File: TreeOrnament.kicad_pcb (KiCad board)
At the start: 2 copper layers, 13 parts, among them J1 USB_B_Micro

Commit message: xmas tree outline
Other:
- board outline added: 20 x 45 mm
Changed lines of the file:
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@@
     (links 18)
     (no_connects 18)
-    (area 0 0 0 0)
+    (area 123.825 100.965 160.875002 124.875)
     (thickness 1.6)
-    (drawings 0)
+    (drawings 5)
     (tracks 0)
     (zones 0)
@@
     )
   )
+  (gr_line (start 125 70) (end 115 85) (angle 90) (layer Edge.Cuts) (width 0.15))
+  (gr_line (start 120 70) (end 125 70) (angle 90) (layer Edge.Cuts) (width 0.15))
+  (gr_line (start 130 55) (end 120 70) (angle 90) (layer Edge.Cuts) (width 0.15))
+  (gr_line (start 125 55) (end 130 55) (angle 90) (layer Edge.Cuts) (width 0.15))
+  (gr_line (start 135 40) (end 125 55) (angle 90) (layer Edge.Cuts) (width 0.15))
 )

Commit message: draw the tree
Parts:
- J1: moved to B.Cu
- moved D5 59.0 mm to (195.0, 150.0)
- moved D2 50.0 mm to (165.4, 159.0)
- moved D1 50.0 mm to (176.4, 144.9)
- moved D3 50.0 mm to (181.7, 144.9)
- moved D4 50.0 mm to (175.6, 152.9)
- moved D6 50.0 mm to (180.9, 152.9)
- moved D7 50.0 mm to (170.7, 160.8)
- moved D8 50.0 mm to (186.2, 152.9)
- moved R1 19.5 mm to (115.0, 95.0), turned to 330 degrees
- moved R3 16.6 mm to (135.0, 105.0), turned to 330 degrees
- moved J1 16.0 mm to (135.0, 90.0)
- moved R2 11.8 mm to (125.0, 100.0), turned to 330 degrees
- moved R4 9.85 mm to (145.0, 110.0), turned to 330 degrees
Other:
- board size 20 x 45 mm -> 80 x 105 mm

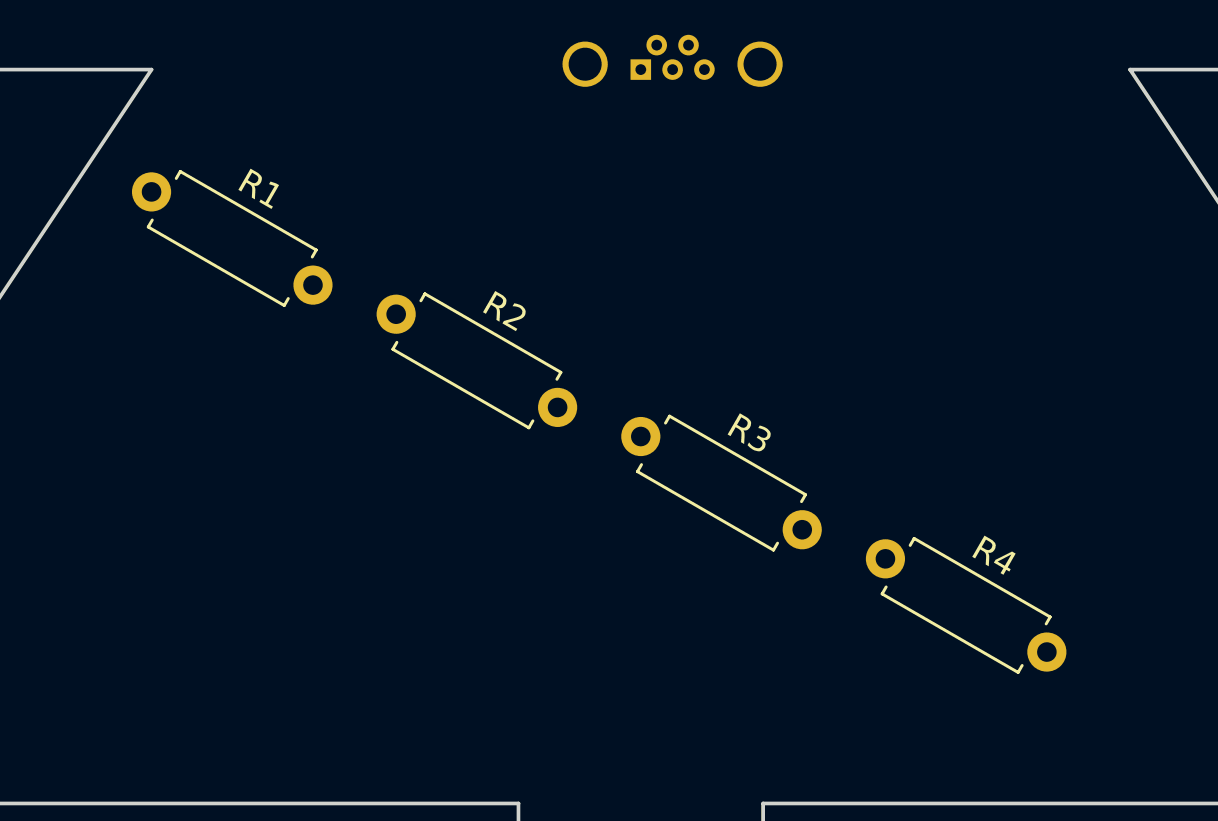
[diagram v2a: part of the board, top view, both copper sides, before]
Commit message: change angle of resistors
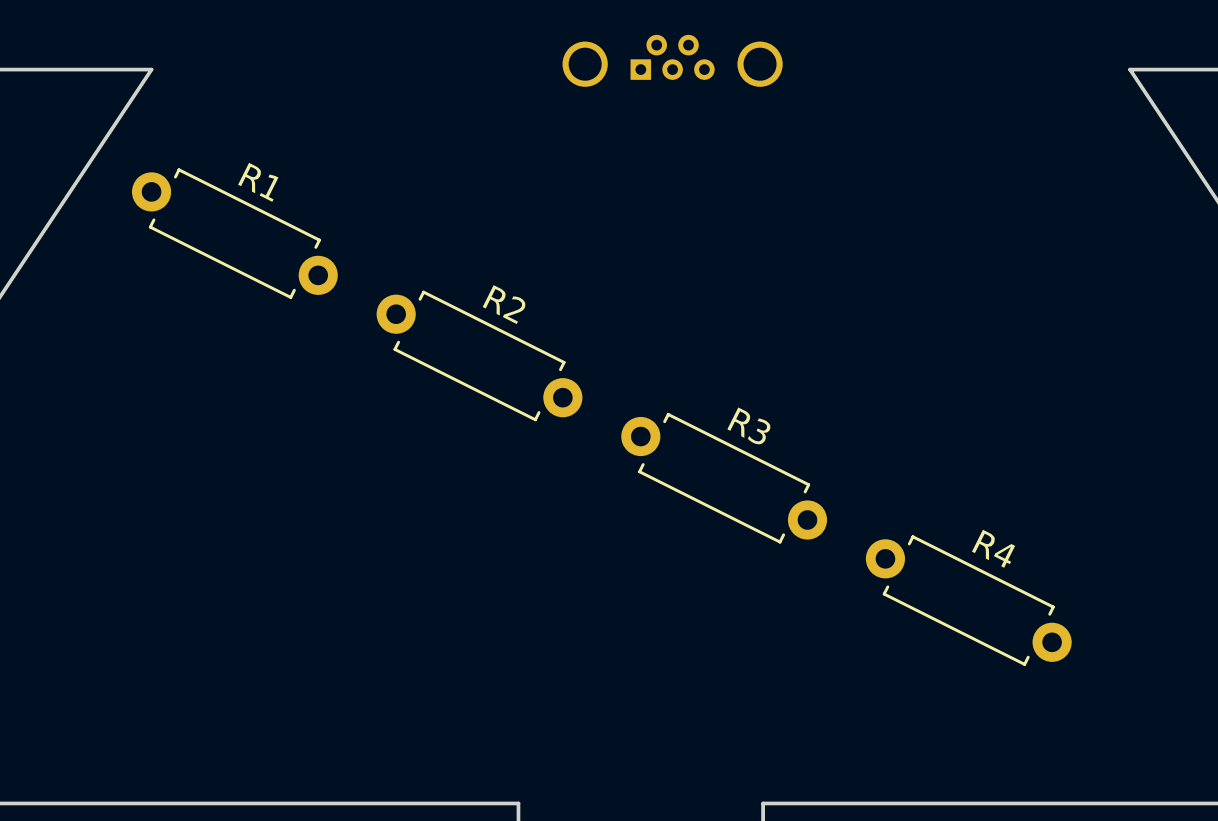
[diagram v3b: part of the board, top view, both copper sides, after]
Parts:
- turned R1 to 333.4 degrees
- turned R2 to 333.4 degrees
- turned R3 to 333.4 degrees
- turned R4 to 333.4 degrees
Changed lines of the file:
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@@
   )
   (module Resistors_THT:R_Axial_DIN0207_L6.3mm_D2.5mm_P7.62mm_Horizontal (layer F.Cu)
-    (at 115 95 330)
+    (at 115 95 333.4)
     (descr "Resistor, Axial_DIN0207 series, Axial, Horizontal, pin pitch=7.62mm, 0.25W = 1/4W, length*diameter=6.3*2.5mm^2, http://cdn-reichelt.de/documents/datenblatt/B400/1_4W%23YAG.pdf")
     (tags "Resistor Axial_DIN0207 series Axial Horizontal pin pitch 7.62mm 0.25W = 1/4W length 6.3mm diameter 2.5mm")
-    (fp_text reference R1 (at 3.81 -2.31 330) (layer F.SilkS)
+    (fp_text reference R1 (at 3.81 -2.31 333.4) (layer F.SilkS)
       (effects (font (size 1 1) (thickness 0.15)))
     )
-    (fp_text value 56 (at 3.81 2.31 330) (layer F.Fab)
+    (fp_text value 56 (at 3.81 2.31 333.4) (layer F.Fab)
       (effects (font (size 1 1) (thickness 0.15)))
     )
@@
     (fp_line (start 8.7 1.6) (end 8.7 -1.6) (layer F.CrtYd) (width 0.05))
     (fp_line (start 8.7 -1.6) (end -1.05 -1.6) (layer F.CrtYd) (width 0.05))
-    (pad 1 thru_hole circle (at 0 0 330) (size 1.6 1.6) (drill 0.8) (layers *.Cu *.Mask)
+    (pad 1 thru_hole circle (at 0 0 333.4) (size 1.6 1.6) (drill 0.8) (layers *.Cu *.Mask)
       (net 10 +5V))
-    (pad 2 thru_hole oval (at 7.62 0 330) (size 1.6 1.6) (drill 0.8) (layers *.Cu *.Mask)
+    (pad 2 thru_hole oval (at 7.62 0 333.4) (size 1.6 1.6) (drill 0.8) (layers *.Cu *.Mask)
       (net 3 "Net-(D2-Pad2)"))
     (model ${KISYS3DMOD}/Resistors_THT.3dshapes/R_Axial_DIN0207_L6.3mm_D2.5mm_P7.62mm_Horizontal.wrl
@@
   )
   (module Resistors_THT:R_Axial_DIN0207_L6.3mm_D2.5mm_P7.62mm_Horizontal (layer F.Cu)
-    (at 125 100 330)
+    (at 125 100 333.4)
     (descr "Resistor, Axial_DIN0207 series, Axial, Horizontal, pin pitch=7.62mm, 0.25W = 1/4W, length*diameter=6.3*2.5mm^2, http://cdn-reichelt.de/documents/datenblatt/B400/1_4W%23YAG.pdf")
     (tags "Resistor Axial_DIN0207 series Axial Horizontal pin pitch 7.62mm 0.25W = 1/4W length 6.3mm diameter 2.5mm")
-    (fp_text reference R2 (at 3.81 -2.31 330) (layer F.SilkS)
+    (fp_text reference R2 (at 3.81 -2.31 333.4) (layer F.SilkS)
       (effects (font (size 1 1) (thickness 0.15)))
     )
-    (fp_text value 56 (at 3.81 2.31 330) (layer F.Fab)
+    (fp_text value 56 (at 3.81 2.31 333.4) (layer F.Fab)
       (effects (font (size 1 1) (thickness 0.15)))
     )
@@
     (fp_line (start 8.7 1.6) (end 8.7 -1.6) (layer F.CrtYd) (width 0.05))
     (fp_line (start 8.7 -1.6) (end -1.05 -1.6) (layer F.CrtYd) (width 0.05))
-    (pad 1 thru_hole circle (at 0 0 330) (size 1.6 1.6) (drill 0.8) (layers *.Cu *.Mask)
+    (pad 1 thru_hole circle (at 0 0 333.4) (size 1.6 1.6) (drill 0.8) (layers *.Cu *.Mask)
       (net 10 +5V))
-    (pad 2 thru_hole oval (at 7.62 0 330) (size 1.6 1.6) (drill 0.8) (layers *.Cu *.Mask)
+    (pad 2 thru_hole oval (at 7.62 0 333.4) (size 1.6 1.6) (drill 0.8) (layers *.Cu *.Mask)
       (net 5 "Net-(D4-Pad2)"))
     (model ${KISYS3DMOD}/Resistors_THT.3dshapes/R_Axial_DIN0207_L6.3mm_D2.5mm_P7.62mm_Horizontal.wrl
@@
   )
   (module Resistors_THT:R_Axial_DIN0207_L6.3mm_D2.5mm_P7.62mm_Horizontal (layer F.Cu)
-    (at 135 105 330)
+    (at 135 105 333.4)
     (descr "Resistor, Axial_DIN0207 series, Axial, Horizontal, pin pitch=7.62mm, 0.25W = 1/4W, length*diameter=6.3*2.5mm^2, http://cdn-reichelt.de/documents/datenblatt/B400/1_4W%23YAG.pdf")
     (tags "Resistor Axial_DIN0207 series Axial Horizontal pin pitch 7.62mm 0.25W = 1/4W length 6.3mm diameter 2.5mm")
-    (fp_text reference R3 (at 3.81 -2.31 330) (layer F.SilkS)
+    (fp_text reference R3 (at 3.81 -2.31 333.4) (layer F.SilkS)
       (effects (font (size 1 1) (thickness 0.15)))
     )
-    (fp_text value 56 (at 3.81 2.31 330) (layer F.Fab)
+    (fp_text value 56 (at 3.81 2.31 333.4) (layer F.Fab)
       (effects (font (size 1 1) (thickness 0.15)))
     )
@@
     (fp_line (start 8.7 1.6) (end 8.7 -1.6) (layer F.CrtYd) (width 0.05))
     (fp_line (start 8.7 -1.6) (end -1.05 -1.6) (layer F.CrtYd) (width 0.05))
-    (pad 1 thru_hole circle (at 0 0 330) (size 1.6 1.6) (drill 0.8) (layers *.Cu *.Mask)
+    (pad 1 thru_hole circle (at 0 0 333.4) (size 1.6 1.6) (drill 0.8) (layers *.Cu *.Mask)
       (net 10 +5V))
-    (pad 2 thru_hole oval (at 7.62 0 330) (size 1.6 1.6) (drill 0.8) (layers *.Cu *.Mask)
+    (pad 2 thru_hole oval (at 7.62 0 333.4) (size 1.6 1.6) (drill 0.8) (layers *.Cu *.Mask)
       (net 7 "Net-(D6-Pad2)"))
     (model ${KISYS3DMOD}/Resistors_THT.3dshapes/R_Axial_DIN0207_L6.3mm_D2.5mm_P7.62mm_Horizontal.wrl
@@
   )
   (module Resistors_THT:R_Axial_DIN0207_L6.3mm_D2.5mm_P7.62mm_Horizontal (layer F.Cu)
-    (at 145 110 330)
+    (at 145 110 333.4)
     (descr "Resistor, Axial_DIN0207 series, Axial, Horizontal, pin pitch=7.62mm, 0.25W = 1/4W, length*diameter=6.3*2.5mm^2, http://cdn-reichelt.de/documents/datenblatt/B400/1_4W%23YAG.pdf")
     (tags "Resistor Axial_DIN0207 series Axial Horizontal pin pitch 7.62mm 0.25W = 1/4W length 6.3mm diameter 2.5mm")
-    (fp_text reference R4 (at 3.81 -2.31 330) (layer F.SilkS)
+    (fp_text reference R4 (at 3.81 -2.31 333.4) (layer F.SilkS)
       (effects (font (size 1 1) (thickness 0.15)))
     )
-    (fp_text value 56 (at 3.81 2.31 330) (layer F.Fab)
+    (fp_text value 56 (at 3.81 2.31 333.4) (layer F.Fab)
       (effects (font (size 1 1) (thickness 0.15)))
     )
@@
     (fp_line (start 8.7 1.6) (end 8.7 -1.6) (layer F.CrtYd) (width 0.05))
     (fp_line (start 8.7 -1.6) (end -1.05 -1.6) (layer F.CrtYd) (width 0.05))
-    (pad 1 thru_hole circle (at 0 0 330) (size 1.6 1.6) (drill 0.8) (layers *.Cu *.Mask)
+    (pad 1 thru_hole circle (at 0 0 333.4) (size 1.6 1.6) (drill 0.8) (layers *.Cu *.Mask)
       (net 10 +5V))
-    (pad 2 thru_hole oval (at 7.62 0 330) (size 1.6 1.6) (drill 0.8) (layers *.Cu *.Mask)
+    (pad 2 thru_hole oval (at 7.62 0 333.4) (size 1.6 1.6) (drill 0.8) (layers *.Cu *.Mask)
       (net 9 "Net-(D8-Pad2)"))
     (model ${KISYS3DMOD}/Resistors_THT.3dshapes/R_Axial_DIN0207_L6.3mm_D2.5mm_P7.62mm_Horizontal.wrl

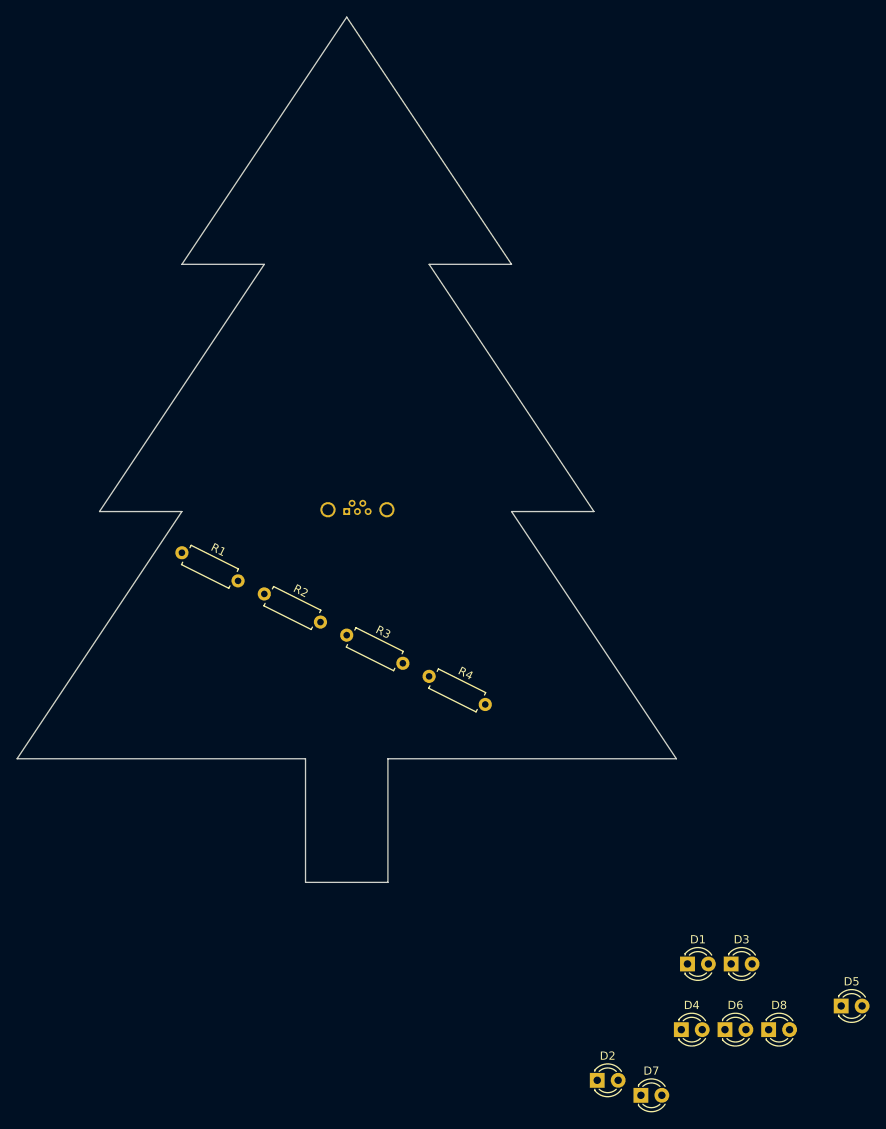
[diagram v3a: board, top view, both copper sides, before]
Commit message: place LEDs on tree
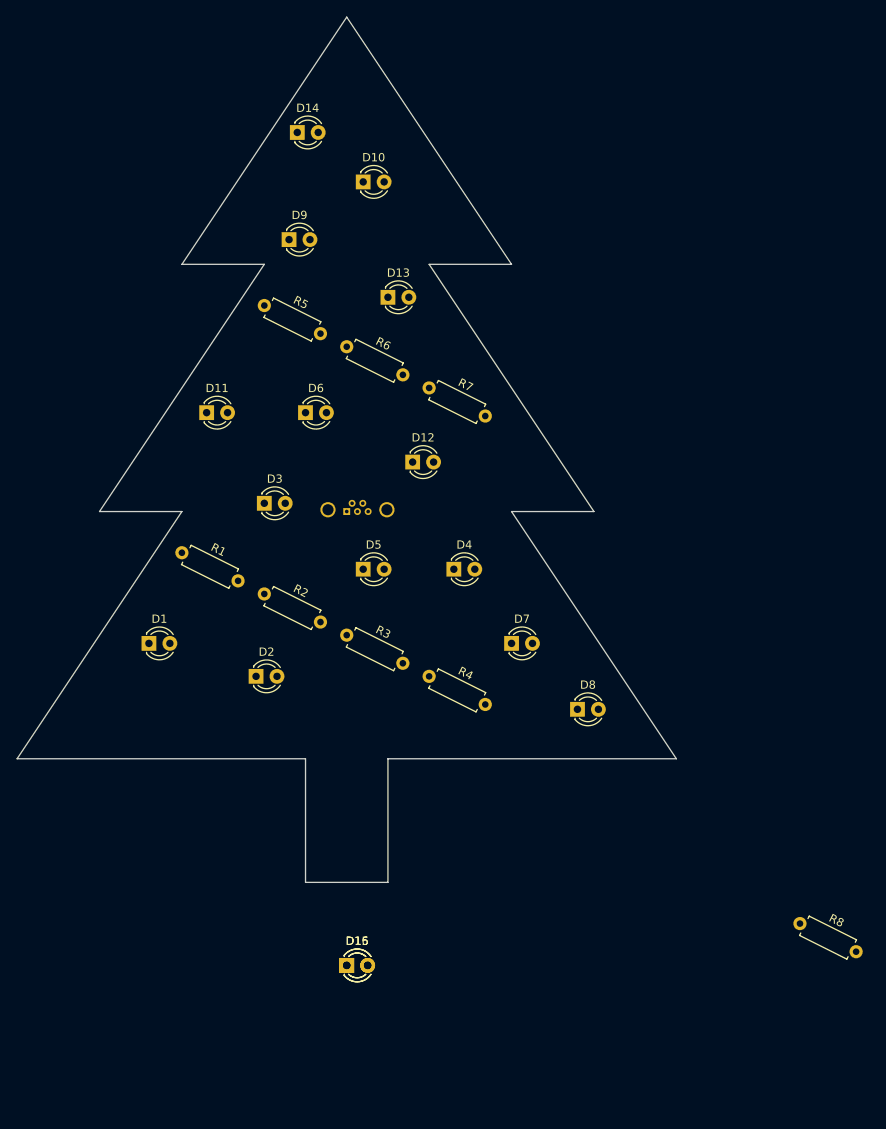
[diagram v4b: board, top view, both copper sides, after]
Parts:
- added D10: LED, LEDs:LED_D3.0mm, F.Cu at (137.0, 50.0)
- added D11: LED, LEDs:LED_D3.0mm, F.Cu at (118.0, 78.0)
- added D12: LED, LEDs:LED_D3.0mm, F.Cu at (143.0, 84.0)
- added D13: LED, LEDs:LED_D3.0mm, F.Cu at (140.0, 64.0)
- added D14: LED, LEDs:LED_D3.0mm, F.Cu at (129.0, 44.0)
- added D15, D16: LED, LEDs:LED_D3.0mm, F.Cu at (135.0, 145.1)
- added D9: LED, LEDs:LED_D3.0mm, F.Cu at (128.0, 57.0)
- added R5: 56, Resistors_THT:R_Axial_DIN0207_L6.3mm_D2.5mm_P7.62mm_Horizontal, F.Cu at (125.0, 65.0)
- added R6: 56, Resistors_THT:R_Axial_DIN0207_L6.3mm_D2.5mm_P7.62mm_Horizontal, F.Cu at (135.0, 70.0)
- added R7: 56, Resistors_THT:R_Axial_DIN0207_L6.3mm_D2.5mm_P7.62mm_Horizontal, F.Cu at (145.0, 75.0)
- added R8: 56, Resistors_THT:R_Axial_DIN0207_L6.3mm_D2.5mm_P7.62mm_Horizontal, F.Cu at (190.0, 140.0)
- moved D6 90.5 mm to (130.0, 78.0)
- moved D3 79.6 mm to (125.0, 89.0)
- moved D5 78.6 mm to (137.0, 97.0)
- moved D1 76.1 mm to (111.0, 106.0)
- moved D2 64.2 mm to (124.0, 110.0)
- moved D4 62.3 mm to (148.0, 97.0)
- moved D7 57.0 mm to (155.0, 106.0)
- moved D8 45.3 mm to (163.0, 114.0)
